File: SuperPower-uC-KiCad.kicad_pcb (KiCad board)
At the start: 4 copper layers, 45.1 x 45.1 mm, 5 parts, among them J5 Conn_01x14_Female, J6 Conn_01x14_Female, J9 MCU board

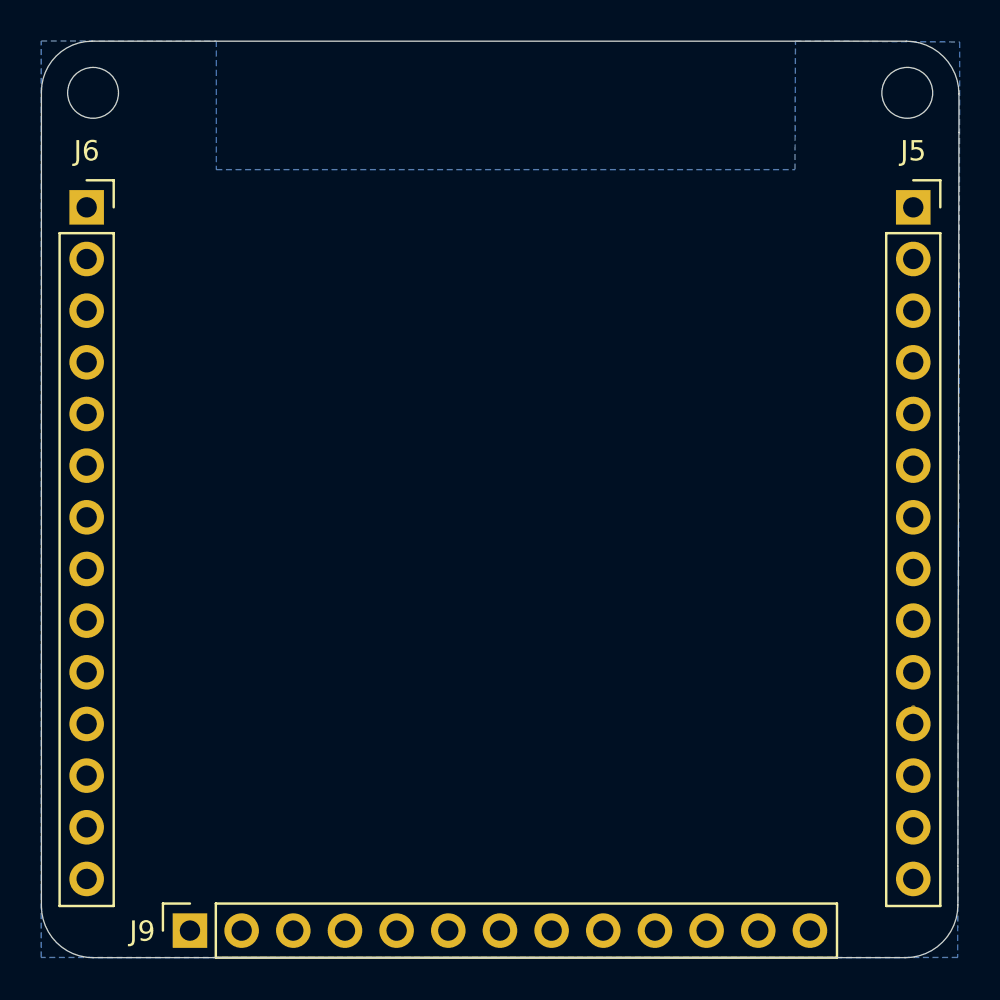
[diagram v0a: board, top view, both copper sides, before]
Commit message: Add copper area to top layer as well
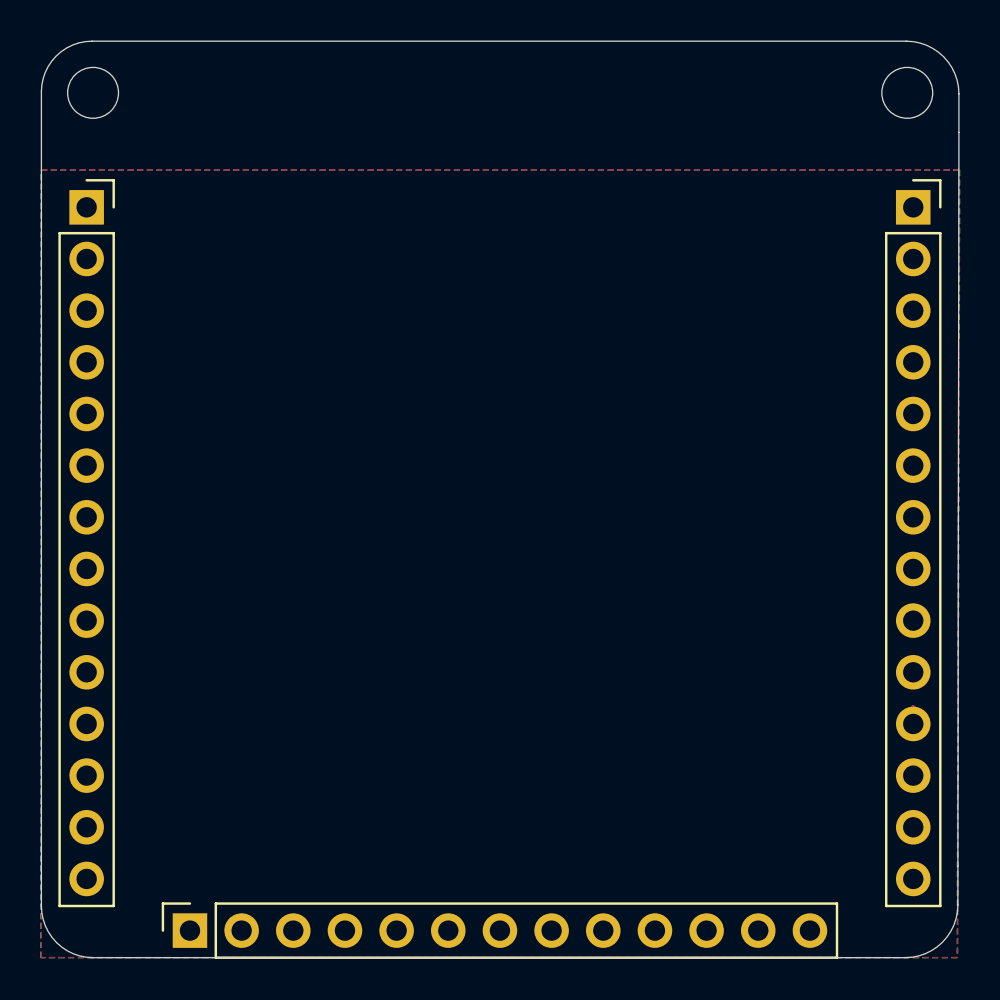
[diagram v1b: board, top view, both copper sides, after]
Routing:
- added copper zone on B.Cu, net (none)
- added copper zone on F.Cu, net GND
- removed copper zone on B.Cu, net GND
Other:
- board text removed: "EN"
- board text removed: "G12"
- board text removed: "G13"
- board text removed: "G14"
- board text removed: "G25"
- board text removed: "G26"
- board text removed: "G27"
- board text removed: "G32"
- board text removed: "G33"
- board text removed: "G34"
- board text removed: "G35"
- board text removed: "G36"
- board text removed: "G39"
- board text removed: "GND"
